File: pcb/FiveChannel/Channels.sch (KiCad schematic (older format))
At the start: 20 parts, among them J201 Power Out, J202 NeoPixel Data, J203 Power Out, J204 NeoPixel Data, J205 Power Out, J206 NeoPixel Data, J207 Power Out, J208 NeoPixel Data, J209 Power Out, J210 NeoPixel Data

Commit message: Started the layout
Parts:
- J201, J202, J203, J204, J205, J206, J207, J208, J209, J210: footprint Pin_Headers:Pin_Header_Straight_1x02_Pitch2.54mm -> Wire_Connections_Bridges:WireConnection_0.80mmDrill
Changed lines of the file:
@@
 F 0 "J202" H 3700 1850 50  0000 C CNN
 F 1 "NeoPixel Data" H 3350 1700 50  0000 C CNN
-F 2 "Pin_Headers:Pin_Header_Straight_1x02_Pitch2.54mm" H 3700 1750 50  0001 C CNN
+F 2 "Wire_Connections_Bridges:WireConnection_0.80mmDrill" H 3700 1750 50  0001 C CNN
 F 3 "" H 3700 1750 50  0001 C CNN
 	1    3700 1750
@@
 F 0 "J201" H 5200 1800 50  0000 C CNN
 F 1 "Power Out" H 5350 1500 50  0000 C CNN
-F 2 "Pin_Headers:Pin_Header_Straight_1x02_Pitch2.54mm" H 5150 1700 50  0001 C CNN
+F 2 "Wire_Connections_Bridges:WireConnection_0.80mmDrill" H 5150 1700 50  0001 C CNN
 F 3 "" H 5150 1700 50  0001 C CNN
 	1    5150 1700
@@
 F 0 "J204" H 3700 2950 50  0000 C CNN
 F 1 "NeoPixel Data" H 3350 2800 50  0000 C CNN
-F 2 "Pin_Headers:Pin_Header_Straight_1x02_Pitch2.54mm" H 3700 2850 50  0001 C CNN
+F 2 "Wire_Connections_Bridges:WireConnection_0.80mmDrill" H 3700 2850 50  0001 C CNN
 F 3 "" H 3700 2850 50  0001 C CNN
 	1    3700 2850
@@
 F 0 "J203" H 5200 2900 50  0000 C CNN
 F 1 "Power Out" H 5350 2600 50  0000 C CNN
-F 2 "Pin_Headers:Pin_Header_Straight_1x02_Pitch2.54mm" H 5150 2800 50  0001 C CNN
+F 2 "Wire_Connections_Bridges:WireConnection_0.80mmDrill" H 5150 2800 50  0001 C CNN
 F 3 "" H 5150 2800 50  0001 C CNN
 	1    5150 2800
@@
 F 0 "J206" H 3700 4000 50  0000 C CNN
 F 1 "NeoPixel Data" H 3350 3850 50  0000 C CNN
-F 2 "Pin_Headers:Pin_Header_Straight_1x02_Pitch2.54mm" H 3700 3900 50  0001 C CNN
+F 2 "Wire_Connections_Bridges:WireConnection_0.80mmDrill" H 3700 3900 50  0001 C CNN
 F 3 "" H 3700 3900 50  0001 C CNN
 	1    3700 3900
@@
 F 0 "J205" H 5200 3950 50  0000 C CNN
 F 1 "Power Out" H 5350 3650 50  0000 C CNN
-F 2 "Pin_Headers:Pin_Header_Straight_1x02_Pitch2.54mm" H 5150 3850 50  0001 C CNN
+F 2 "Wire_Connections_Bridges:WireConnection_0.80mmDrill" H 5150 3850 50  0001 C CNN
 F 3 "" H 5150 3850 50  0001 C CNN
 	1    5150 3850
@@
 F 0 "J208" H 3700 5050 50  0000 C CNN
 F 1 "NeoPixel Data" H 3350 4900 50  0000 C CNN
-F 2 "Pin_Headers:Pin_Header_Straight_1x02_Pitch2.54mm" H 3700 4950 50  0001 C CNN
+F 2 "Wire_Connections_Bridges:WireConnection_0.80mmDrill" H 3700 4950 50  0001 C CNN
 F 3 "" H 3700 4950 50  0001 C CNN
 	1    3700 4950
@@
 F 0 "J207" H 5200 5000 50  0000 C CNN
 F 1 "Power Out" H 5350 4700 50  0000 C CNN
-F 2 "Pin_Headers:Pin_Header_Straight_1x02_Pitch2.54mm" H 5150 4900 50  0001 C CNN
+F 2 "Wire_Connections_Bridges:WireConnection_0.80mmDrill" H 5150 4900 50  0001 C CNN
 F 3 "" H 5150 4900 50  0001 C CNN
 	1    5150 4900
@@
 F 0 "J210" H 3700 6150 50  0000 C CNN
 F 1 "NeoPixel Data" H 3350 6000 50  0000 C CNN
-F 2 "Pin_Headers:Pin_Header_Straight_1x02_Pitch2.54mm" H 3700 6050 50  0001 C CNN
+F 2 "Wire_Connections_Bridges:WireConnection_0.80mmDrill" H 3700 6050 50  0001 C CNN
 F 3 "" H 3700 6050 50  0001 C CNN
 	1    3700 6050
@@
 F 0 "J209" H 5200 6100 50  0000 C CNN
 F 1 "Power Out" H 5350 5800 50  0000 C CNN
-F 2 "Pin_Headers:Pin_Header_Straight_1x02_Pitch2.54mm" H 5150 6000 50  0001 C CNN
+F 2 "Wire_Connections_Bridges:WireConnection_0.80mmDrill" H 5150 6000 50  0001 C CNN
 F 3 "" H 5150 6000 50  0001 C CNN
 	1    5150 6000

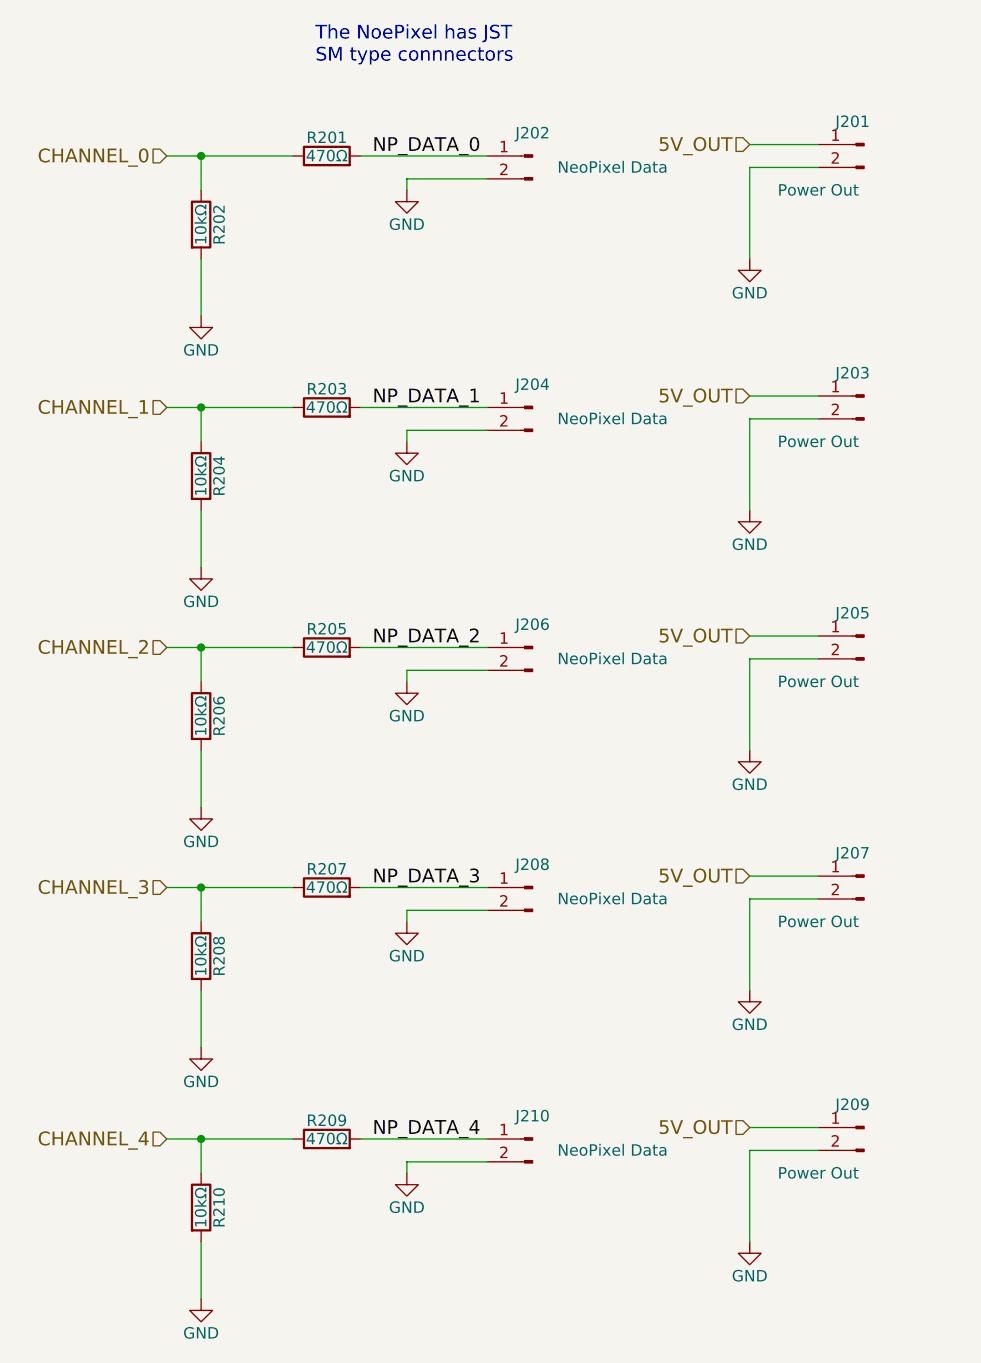
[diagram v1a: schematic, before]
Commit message: Working through the five channel prototype layout
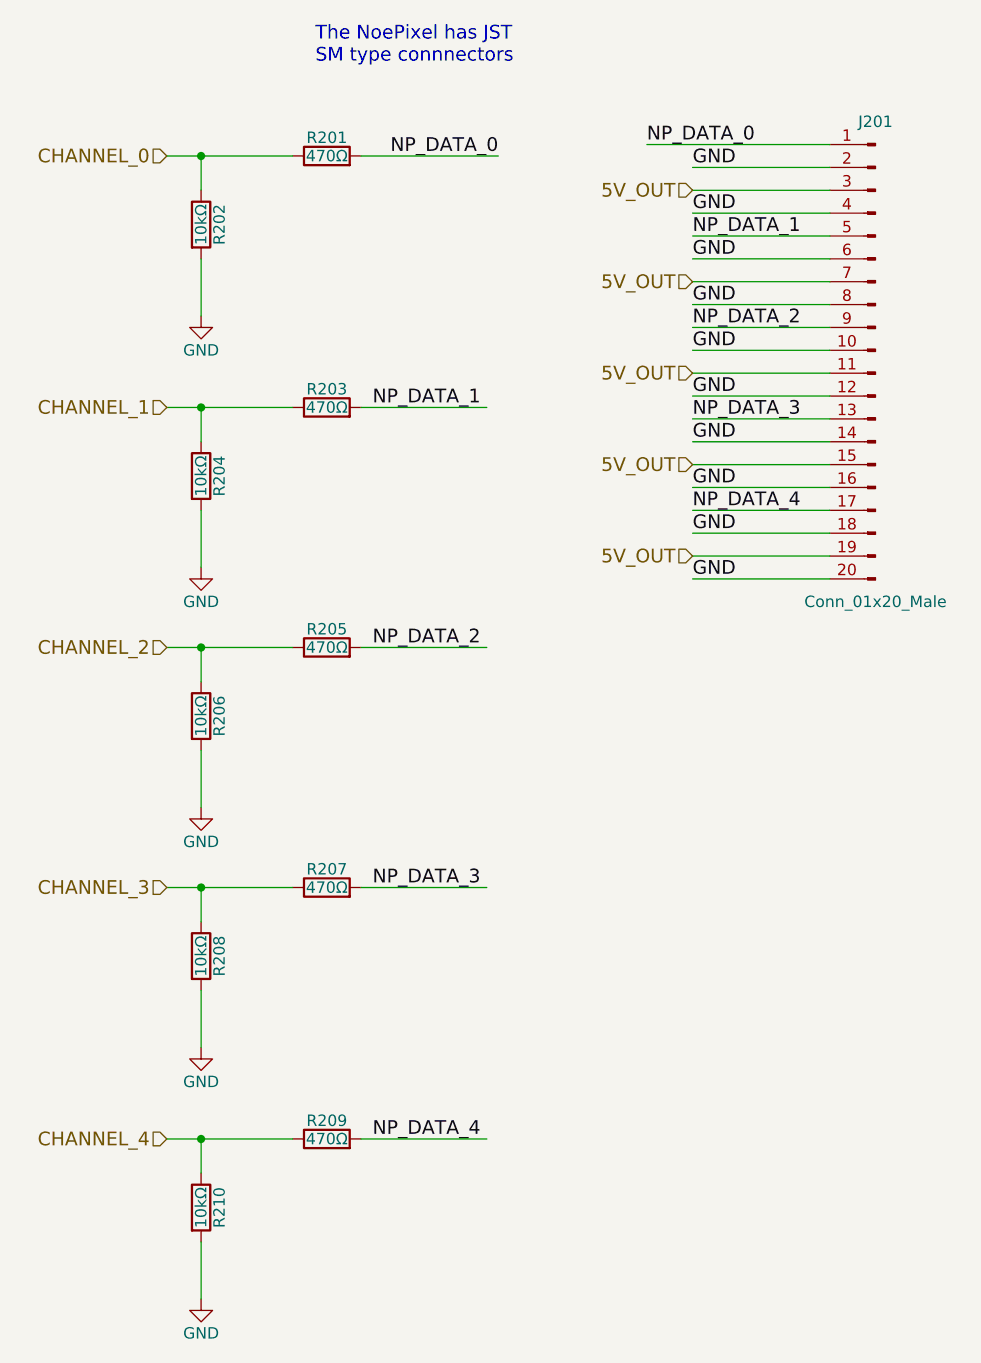
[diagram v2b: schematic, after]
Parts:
- removed J201, J203, J205, J207, J209: Power Out, Wire_Connections_Bridges:WireConnection_0.80mmDrill, symbol Conn_01x02_Male
- removed J202, J204, J206, J208, J210: NeoPixel Data, Wire_Connections_Bridges:WireConnection_0.80mmDrill, symbol Conn_01x02_Male
- added J201: Conn_01x20_Male, Pin_Headers:Pin_Header_Angled_2x10_Pitch2.54mm, symbol Conn_01x20_Male
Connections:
- wire segments 45 -> 40
